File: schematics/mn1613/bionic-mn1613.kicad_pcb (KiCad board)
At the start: 2 copper layers, 48.3 x 71.1 mm, 10 parts, among them J1 Bionic-P135, J2 Bionic-P245, U1 MN1613, U2 74HCT126, U3 11AA010-I/TO

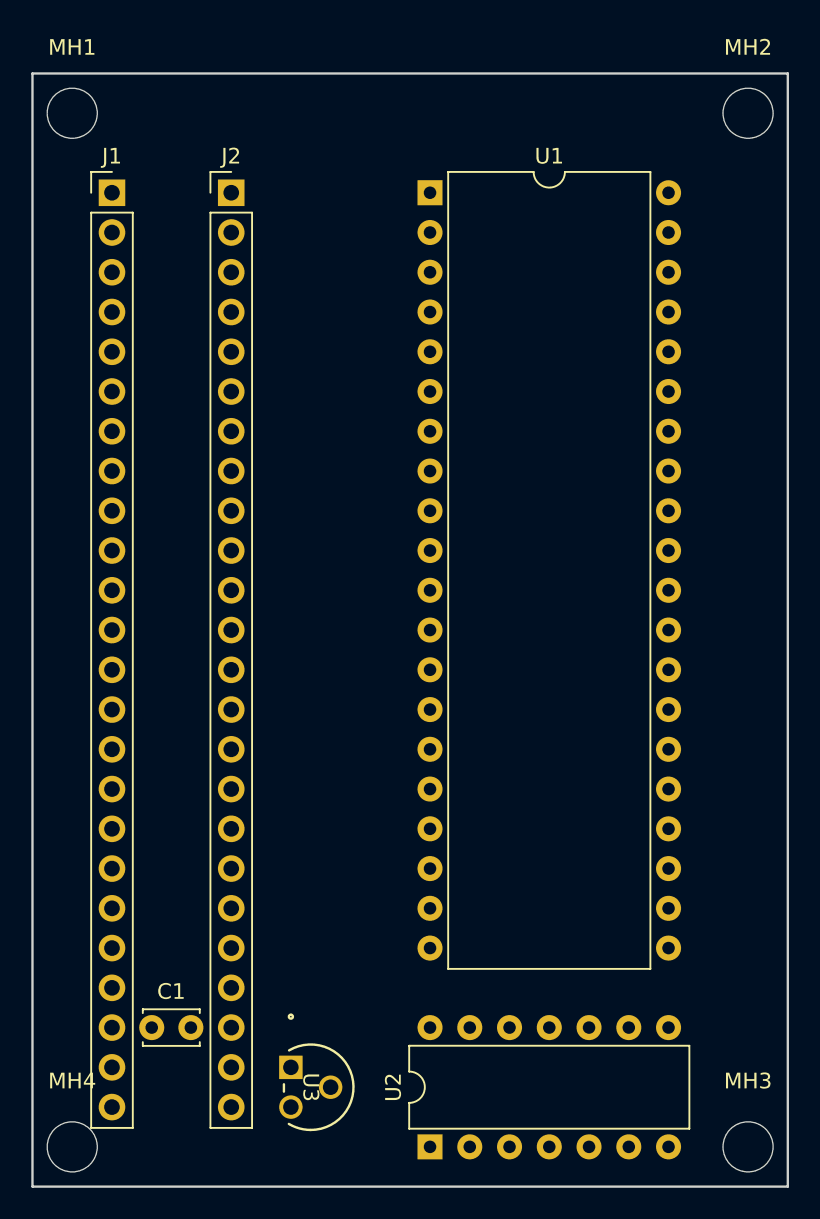
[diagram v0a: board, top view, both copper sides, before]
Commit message: [MN1613] Update schematics
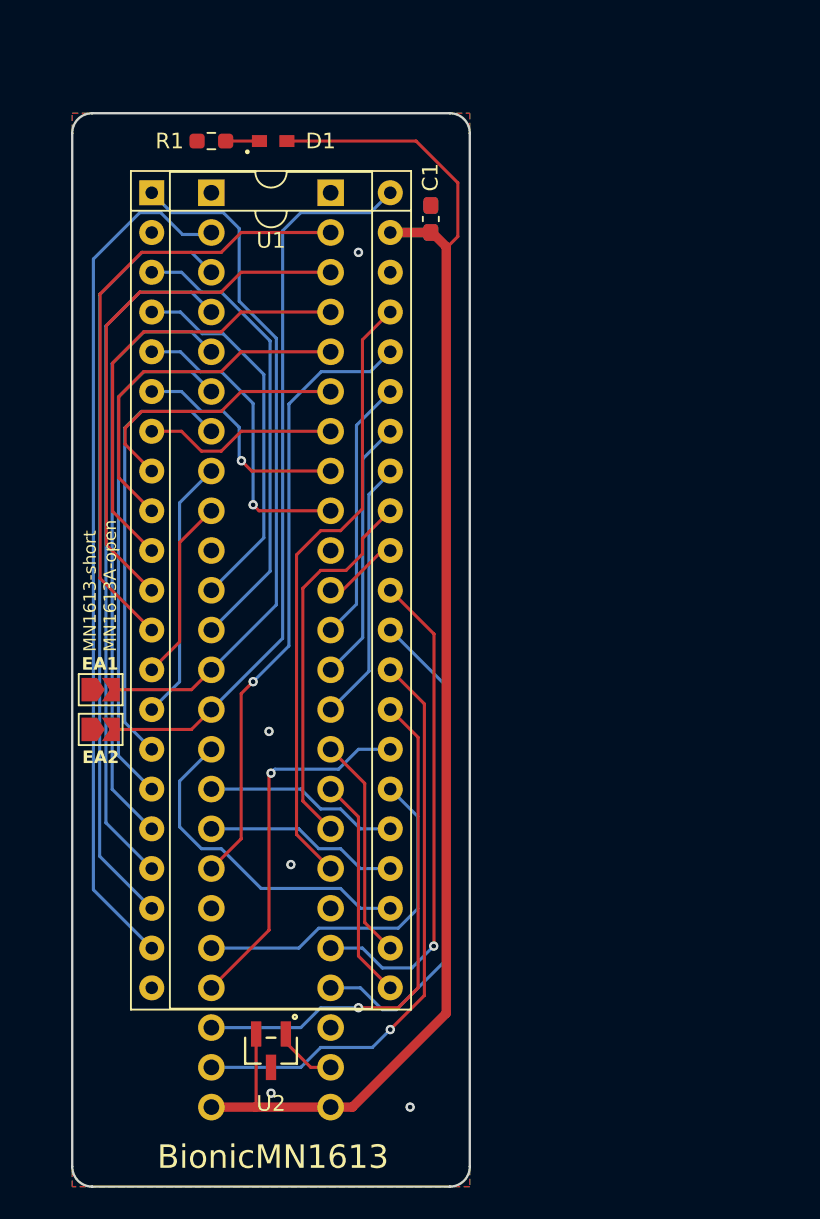
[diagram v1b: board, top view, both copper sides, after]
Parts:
- removed MH1, MH2, MH3, MH4: MountingHole_3.2mm_M3, MountingHole:MountingHole_3.2mm_M3
- removed U3: 11AA010-I/TO, microchip:TO-92_MC_MCH
- added C2: 22u, Capacitor_SMD:C_0603_1608Metric_Pad1.08x0.95mm_HandSolder, B.Cu at (123.9, 76.8)
- added D1: CSL1901UW1, 0-LocalLibrary:LED_CSL1901UW1_ROM-M, F.Cu at (113.8, 71.8)
- added EA1: EA1, Jumper:SolderJumper-2_P1.3mm_Open_TrianglePad1.0x1.5mm, F.Cu at (102.8, 106.8)
- added EA2: EA2, Jumper:SolderJumper-2_P1.3mm_Open_TrianglePad1.0x1.5mm, F.Cu at (102.8, 109.4)
- added R1: 1.6k, Resistor_SMD:R_0603_1608Metric_Pad0.98x0.95mm_HandSolder, F.Cu at (109.9, 71.8)
- C1: footprint Capacitor_THT:C_Disc_D3.4mm_W2.1mm_P2.50mm -> Capacitor_SMD:C_0603_1608Metric_Pad1.08x0.95mm_HandSolder
- J1: footprint connector:Bionic-P135_Vertical -> 0-LocalLibrary:Bionic-P135_Vertical; moved to B.Cu
- J2: footprint connector:Bionic-P245_Vertical -> 0-LocalLibrary:Bionic-P245_Vertical; moved to B.Cu
- U1: value MN1613 -> MN1613A; footprint Package_DIP:DIP-40_W15.24mm -> 0-LocalLibrary:DIP-42_W15.24mm_Socket
- U2: value 74HCT126 -> 11AA010-I/TT; footprint Package_DIP:DIP-14_W7.62mm -> 0-LocalLibrary:SOT-23_MC_MCH-M
- moved C1 54.7 mm to (123.9, 76.8), turned to 90 degrees
- moved U1 17.8 mm to (106.1, 75.1)
- moved U2 11.9 mm to (113.7, 129.9), turned to 180 degrees
- moved J2 6.35 mm to (117.5, 75.1), turned to 180 degrees
- moved J1 6.35 mm to (109.9, 75.1), turned to 180 degrees
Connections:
- J1 pad 13: unconnected-(J1-P32-Pad13) -> /P32
- J1 pad 14: unconnected-(J1-P33-Pad14) -> /P33
- J2 pad 29: unconnected-(J2-P54-Pad29) -> /P54
- U1 pad 1: /P55 -> /P32
- U1 pad 10: /P21 -> /P22
- U1 pad 11: /P20 -> /P21
- U1 pad 12: /P17 -> /P20
- U1 pad 13: /P16 -> /P17
- U1 pad 14: /P15 -> /P16
- U1 pad 15: /P14 -> /P15
- U1 pad 16: /P13 -> /P14
- U1 pad 17: /P12 -> /P13
- U1 pad 18: /P11 -> /P12
- U1 pad 19: /P10 -> /P11
- U1 pad 2: /P31 -> unconnected-(U1-~{OE}-Pad2)
- U1 pad 20: GND -> /P10
- U1 pad 21: unconnected-(U1-~{ST}-Pad21) -> GND
- U1 pad 22: unconnected-(U1-~{SD}-Pad22) -> /P45
- U1 pad 23: /P50 -> /P44
- U1 pad 24: /P52 -> /P34
- U1 pad 25: /P51 -> /P36
- U1 pad 26: /P37 -> /P35
- U1 pad 27: /P36 -> /P50
- U1 pad 28: /P35 -> /P51
- U1 pad 29: /P53 -> /P52
- U1 pad 3: /P30 -> /P31
- U1 pad 30: /P41 -> /P53
- U1 pad 31: /P43 -> /P55
- U1 pad 32: /P40 -> /P54
- U1 pad 33: /P34 -> /P40
- U1 pad 34: /P45 -> /P46
- U1 pad 35: /P42 -> /P43
- U1 pad 36: /P44 -> /P42
- U1 pad 37: /P47 -> /P41
- U1 pad 38: Net-(U1-X2) -> /P37
- U1 pad 39: unconnected-(U1-X1-Pad39) -> /P47
- U1 pad 4: /P27 -> /P30
- U1 pad 40: VCC -> unconnected-(U1-X1-Pad40)
- U1 pad 5: /P26 -> /P27
- U1 pad 6: /P25 -> /P26
- U1 pad 7: /P24 -> /P25
- U1 pad 8: /P23 -> /P24
- U1 pad 9: /P22 -> /P23
- U2 pad 1: VCC -> Net-(J2-P57)
- U2 pad 2: /P46 -> VCC
- U2 pad 3: Net-(U1-X2) -> GND
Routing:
- net VCC: track 0.00 -> 94.4 mm
- net /P10: track 0.00 -> 55.0 mm
- net /P11: track 0.00 -> 49.4 mm
- net /P33: track 0.00 -> 47.2 mm
- net /P32: track 0.00 -> 44.5 mm
- net /P12: track 0.00 -> 44.0 mm
- net /P47: track 0.00 -> 39.7 mm
- net /P37: track 0.00 -> 39.6 mm, vias 0 -> 1
- net /P20: track 0.00 -> 39.2 mm
- net /P13: track 0.00 -> 38.5 mm
- net /P53: track 0.00 -> 37.2 mm, vias 0 -> 1
- net /P21: track 0.00 -> 33.9 mm
- net /P14: track 0.00 -> 33.1 mm
- net /P52: track 0.00 -> 32.8 mm, vias 0 -> 1
- net /P55: track 0.00 -> 31.8 mm
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- added copper zone on B.Cu, net GND
- added copper zone on F.Cu, net GND
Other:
- board size 48.3 x 71.1 mm -> 25.4 x 68.6 mm
- board text added: "BionicMN1613"
- board text added: "JLCJLCJLCJLC"
- board text added: "MN1613-short MN1613A-open"
- board text added: "Rev. 2"

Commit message: [MN1613] Cleanup schematics
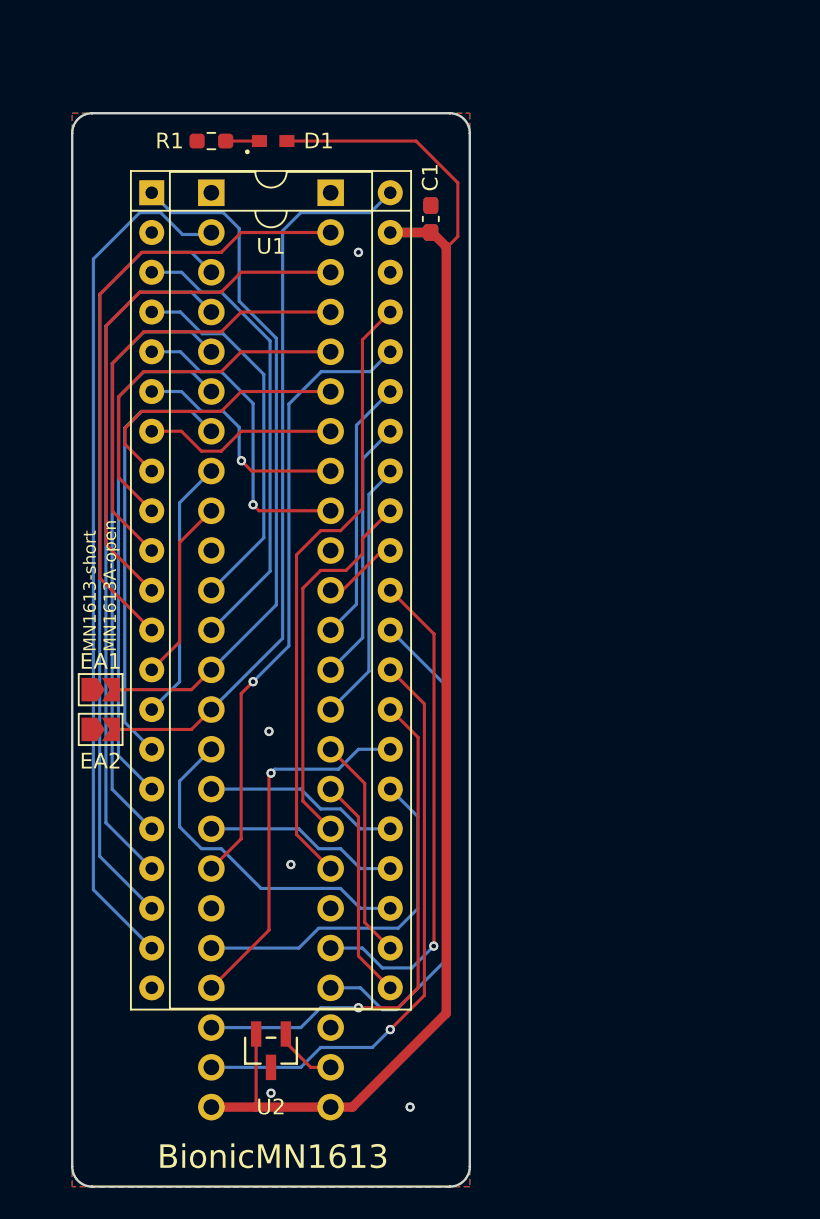
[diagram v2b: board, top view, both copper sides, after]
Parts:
- D1: footprint 0-LocalLibrary:LED_CSL1901UW1_ROM-M -> rhom:LED_CSL1901UW1_ROM-M
- EA1, EA2: footprint Jumper:SolderJumper-2_P1.3mm_Open_TrianglePad1.0x1.5mm -> bionic:SolderJumper-2_P1.3mm_Open_TrianglePad1.0x1.5mm
- J1: footprint 0-LocalLibrary:Bionic-P135_Vertical -> bionic:Bionic-P135_Vertical
- J2: footprint 0-LocalLibrary:Bionic-P245_Vertical -> bionic:Bionic-P245_Vertical
- U1: footprint 0-LocalLibrary:DIP-42_W15.24mm_Socket -> bionic:DIP-42_W15.24mm_Socket
- U2: footprint 0-LocalLibrary:SOT-23_MC_MCH-M -> microchip:SOT-23_MC_MCH-M
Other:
- rule pad_to_mask_clearance: 0.051 -> 0
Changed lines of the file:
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@@
 	)
 	(setup
-		(pad_to_mask_clearance 0.051)
-		(solder_mask_min_width 0.25)
+		(pad_to_mask_clearance 0)
 		(allow_soldermask_bridges_in_footprints no)
 		(aux_axis_origin 101 70)
@@
 	(net 48 "unconnected-(U1-~{OE}-Pad2)")
 	(net 49 "unconnected-(U1-X1-Pad40)")
-	(footprint "Jumper:SolderJumper-2_P1.3mm_Open_TrianglePad1.0x1.5mm"
+	(footprint "bionic:SolderJumper-2_P1.3mm_Open_TrianglePad1.0x1.5mm"
 		(layer "F.Cu")
 		(at 102.815 109.37)
@@
 		(tags "solder jumper open")
 		(property "Reference" "EA2"
-			(at 0 1.778 0)
-			(layer "F.SilkS")
-			(effects
-				(font
-					(size 0.8 0.8)
-					(thickness 0.1)
-					(bold yes)
+			(at 0 2.032 0)
+			(layer "F.SilkS")
+			(effects
+				(font
+					(size 1 1)
+					(thickness 0.15)
 				)
 			)
@@
 			)
 		)
-		(property "Footprint" "Jumper:SolderJumper-2_P1.3mm_Open_TrianglePad1.0x1.5mm"
+		(property "Footprint" "bionic:SolderJumper-2_P1.3mm_Open_TrianglePad1.0x1.5mm"
 			(at 0 0 0)
 			(unlocked yes)
@@
 		)
 	)
-	(footprint "0-LocalLibrary:SOT-23_MC_MCH-M"
+	(footprint "microchip:SOT-23_MC_MCH-M"
 		(layer "F.Cu")
 		(at 113.7 129.894 180)
-		(tags "11aa010t-i/tt ")
+		(descr "Microchip 11AAxxx-I/TT UNI/O 1Kbit Serial EEPROM")
 		(property "Reference" "U2"
-			(at 0 -3.379 0)
+			(at 0 -3.606 0)
 			(unlocked yes)
 			(layer "F.SilkS")
@@
 			)
 		)
-		(property "Footprint" "0-LocalLibrary:SOT-23_MC_MCH-M"
+		(property "Footprint" "microchip:SOT-23_MC_MCH-M"
 			(at 0 0 180)
 			(layer "F.Fab")
@@
 			)
 		)
-		(property "Description" ""
+		(property "Description" "UNI/O Serial EEPROM (1Kbit)"
 			(at 0 0 180)
 			(layer "F.Fab")
@@
 				(type solid)
 			)
-			(layer "F.SilkS")
-		)
-		(fp_circle
-			(center -1.524 2.159)
-			(end -1.397 2.159)
-			(stroke
-				(width 0.1524)
-				(type solid)
-			)
-			(fill none)
 			(layer "F.SilkS")
 		)
@@
 			(pintype "power_in")
 		)
-		(model "${KIPRJMOD}/0-LocalLibrary/SOT-23_MC_MCH.step"
+		(model "${KIPRJMOD}/microchip.pretty/SOT-23_MC_MCH.step"
 			(offset
 				(xyz 0 0 0)
@@
 		)
 	)
-	(footprint "0-LocalLibrary:DIP-42_W15.24mm_Socket"
+	(footprint "bionic:DIP-42_W15.24mm_Socket"
 		(locked yes)
 		(layer "F.Cu")
@@
 		(tags "THT DIP DIL PDIP 2.54mm 15.24mm 600mil Socket")
 		(property "Reference" "U1"
-			(at 7.62 3.048 0)
+			(at 7.62 3.429 0)
 			(layer "F.SilkS")
 			(effects
@@
 			)
 		)
-		(property "Footprint" "0-LocalLibrary:DIP-42_W15.24mm_Socket"
+		(property "Footprint" "bionic:DIP-42_W15.24mm_Socket"
 			(at 0 0 0)
 			(layer "F.Fab")
@@
 			(pintype "output")
 		)
-		(model "${KICAD6_3DMODEL_DIR}/Package_DIP.3dshapes/DIP-42_W15.24mm_Socket.wrl"
+		(model "${KIPRJMOD}/bionic.pretty/110-87-642-41-001101.stp"
 			(offset
-				(xyz 0 0 0)
+				(xyz 7.5 -25.5 1)
 			)
 			(scale
@@
 			)
 			(rotate
-				(xyz 0 0 0)
+				(xyz 90 -180 -180)
 			)
 		)
@@
 		)
 	)
-	(footprint "Jumper:SolderJumper-2_P1.3mm_Open_TrianglePad1.0x1.5mm"
+	(footprint "bionic:SolderJumper-2_P1.3mm_Open_TrianglePad1.0x1.5mm"
 		(layer "F.Cu")
 		(at 102.815 106.83)
@@
 		(tags "solder jumper open")
 		(property "Reference" "EA1"
-			(at -0.037 -1.651 0)
-			(layer "F.SilkS")
-			(effects
-				(font
-					(size 0.8 0.8)
-					(thickness 0.1)
-					(bold yes)
+			(at 0 -1.8 0)
+			(layer "F.SilkS")
+			(effects
+				(font
+					(size 1 1)
+					(thickness 0.15)
 				)
 			)
 		)
 		(property "Value" "EA1"
-			(at -0.037 1.651 0)
-			(layer "F.Fab")
-			(effects
-				(font
-					(size 0.8 0.8)
-					(thickness 0.1)
-				)
-			)
-		)
-		(property "Footprint" "Jumper:SolderJumper-2_P1.3mm_Open_TrianglePad1.0x1.5mm"
+			(at 0 1.9 0)
+			(layer "F.Fab")
+			(effects
+				(font
+					(size 1 1)
+					(thickness 0.15)
+				)
+			)
+		)
+		(property "Footprint" "bionic:SolderJumper-2_P1.3mm_Open_TrianglePad1.0x1.5mm"
 			(at 0 0 0)
 			(unlocked yes)
@@
 		)
 	)
-	(footprint "0-LocalLibrary:LED_CSL1901UW1_ROM-M"
+	(footprint "rhom:LED_CSL1901UW1_ROM-M"
 		(layer "F.Cu")
 		(at 113.8397 71.778)
@@
 		(tags "CSL1901UW1 ")
 		(property "Reference" "D1"
-			(at 3.0353 0 0)
+			(at 2.9083 0 0)
 			(unlocked yes)
 			(layer "F.SilkS")
@@
 			)
 		)
-		(property "Footprint" "0-LocalLibrary:LED_CSL1901UW1_ROM-M"
+		(property "Footprint" "rhom:LED_CSL1901UW1_ROM-M"
 			(at 0 0 0)
 			(layer "F.Fab")
@@
 			)
 		)
-		(model "${KIPRJMOD}/0-LocalLibrary/LED_CSL1901UW1_ROM.step"
+		(model "${KIPRJMOD}/rhom.pretty/LED_CSL1901UW1_ROM.step"
 			(offset
 				(xyz 0 0 0)
@@
 		)
 	)
-	(footprint "0-LocalLibrary:Bionic-P245_Vertical"
+	(footprint "bionic:Bionic-P245_Vertical"
 		(locked yes)
 		(layer "B.Cu")
@@
 			)
 		)
-		(property "Footprint" "0-LocalLibrary:Bionic-P245_Vertical"
-			(at 0 0 180)
-			(layer "F.Fab")
+		(property "Footprint" "bionic:Bionic-P245_Vertical"
+			(at 0 0 0)
+			(layer "B.Fab")
 			(hide yes)
 			(effects
@@
 					(thickness 0.15)
 				)
+				(justify mirror)
 			)
 		)
 		(property "Datasheet" ""
-			(at 0 0 180)
-			(layer "F.Fab")
+			(at 0 0 0)
+			(layer "B.Fab")
 			(hide yes)
 			(effects
@@
 					(thickness 0.15)
 				)
-			)
-		)
-		(property "Description" ""
-			(at 0 0 180)
-			(layer "F.Fab")
+				(justify mirror)
+			)
+		)
+		(property "Description" "Generic connector, single row, 01x24, script generated (kicad-library-utils/schlib/autogen/connector/)"
+			(at 0 0 0)
+			(layer "B.Fab")
 			(hide yes)
 			(effects
@@
 					(thickness 0.15)
 				)
+				(justify mirror)
 			)
 		)
@@
 		)
 	)
-	(footprint "0-LocalLibrary:Bionic-P135_Vertical"
+	(footprint "bionic:Bionic-P135_Vertical"
 		(locked yes)
 		(layer "B.Cu")
@@
 			)
 		)
-		(property "Footprint" "0-LocalLibrary:Bionic-P135_Vertical"
-			(at 0 0 180)
-			(layer "F.Fab")
+		(property "Footprint" "bionic:Bionic-P135_Vertical"
+			(at 0 0 0)
+			(layer "B.Fab")
 			(hide yes)
 			(effects
@@
 					(thickness 0.15)
 				)
+				(justify mirror)
 			)
 		)
 		(property "Datasheet" ""
-			(at 0 0 180)
-			(layer "F.Fab")
+			(at 0 0 0)
+			(layer "B.Fab")
 			(hide yes)
 			(effects
@@
 					(thickness 0.15)
 				)
-			)
-		)
-		(property "Description" ""
-			(at 0 0 180)
-			(layer "F.Fab")
+				(justify mirror)
+			)
+		)
+		(property "Description" "Generic connector, single row, 01x24, script generated (kicad-library-utils/schlib/autogen/connector/)"
+			(at 0 0 0)
+			(layer "B.Fab")
 			(hide yes)
 			(effects
@@
 					(thickness 0.15)
 				)
-			)
-		)
+				(justify mirror)
+			)
+		)

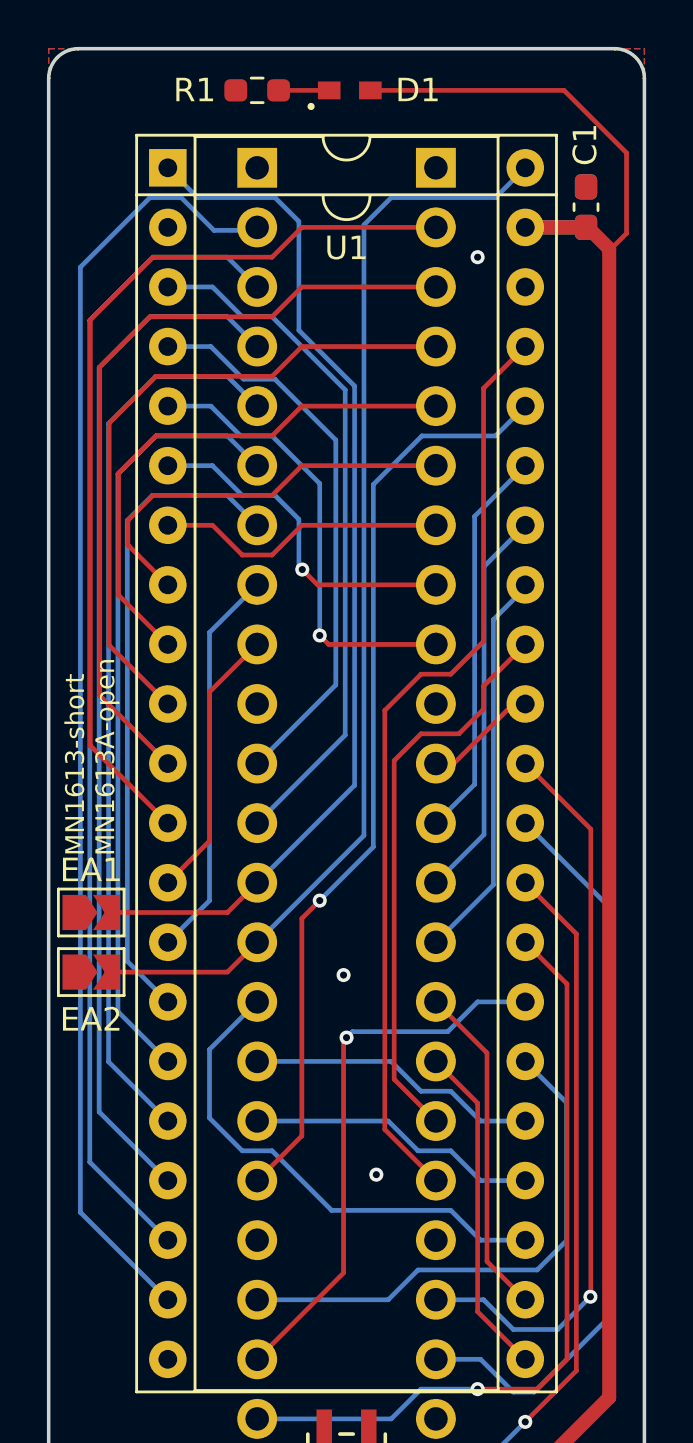
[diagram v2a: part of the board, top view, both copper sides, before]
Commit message: [MN1613] Update schematics
Remove unused pins from bionic connector
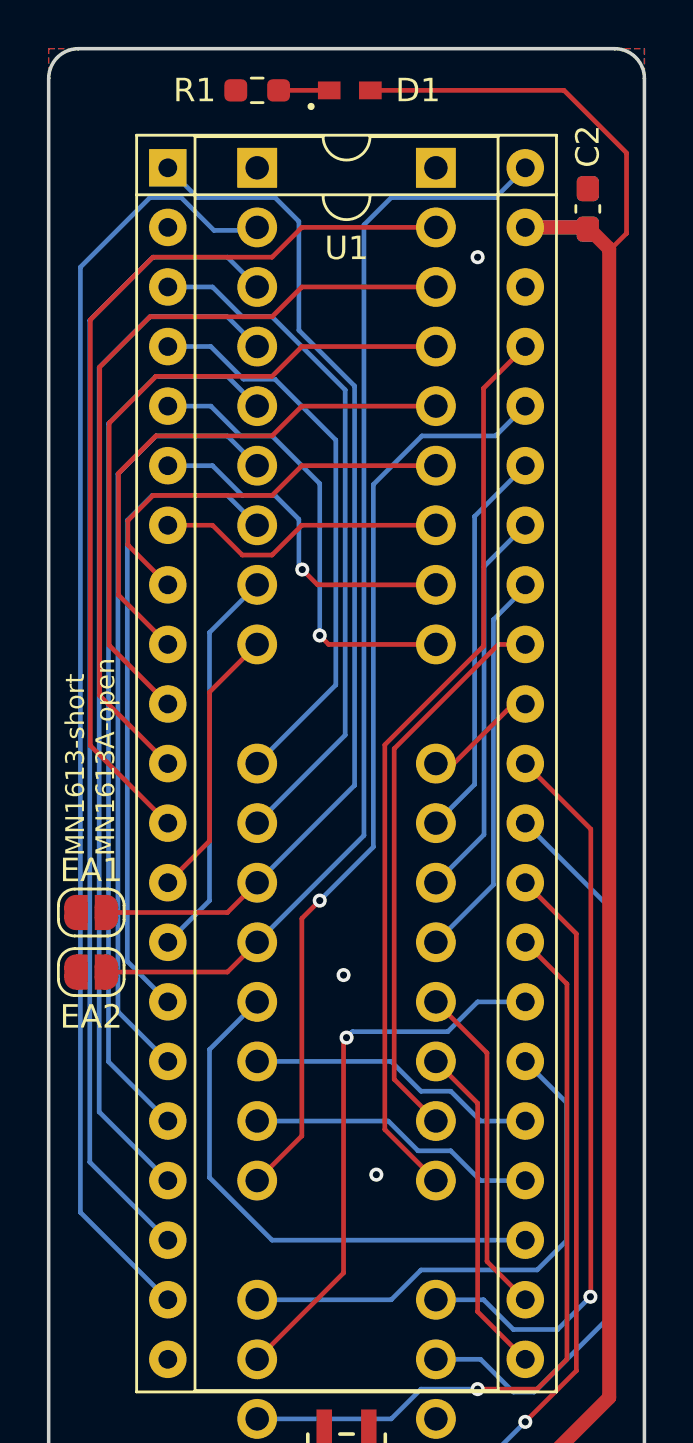
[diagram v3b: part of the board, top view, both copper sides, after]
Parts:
- C1: moved to B.Cu
- C2: moved to F.Cu
- EA1, EA2: footprint bionic:SolderJumper-2_P1.3mm_Open_TrianglePad1.0x1.5mm -> bionic:SolderJumper-2_P1.3mm_Open_RoundedPad1.0x1.5mm
- J1: footprint bionic:Bionic-P135_Vertical -> bionic:Bionic-P135_THT
- J2: footprint bionic:Bionic-P245_Vertical -> bionic:Bionic-P245_THT
- moved C1 0.11 mm to (124.0, 76.8)
- moved C2 0.11 mm to (124.0, 76.8)
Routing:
- net /P34: track 21.4 -> 22.9 mm
- net /P47: track 39.7 -> 38.9 mm
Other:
- board text added: "Rev. 3"
- board text removed: "Rev. 2"
